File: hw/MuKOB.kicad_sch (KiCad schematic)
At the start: 137 parts, among them J1 UART0 IO01, J10 IO_EX, J11 SPKR_L, J12 SPKR_R, J13 UI 20-RBN, J14 AUDIO, J15 SPI-0, J16 SPI-DISP, J17 SW_MATRIX, J18 UIM 20-FCC, J19 UIM 20-RBN, J2 SERIAL-COMM, J3 KEY_SND_IF, J4 GPIO28, J5 I2C-0, J6 MicroSD-Socket w/Det, J7 KEY-PADDLE, J8 UART1 IO89, J9 UI 20-FCC, Q1 2N3904, SW1 RESET, SW2 RE-SO, SW3 UP, SW4 LF, SW5 EN, SW6 RT, SW7 DN, SW8 RE-AO, SW9 RE-BO, U1 MAX3221, U2 PicoW, U3 MCP23S08-E/SO, U4 TLV70033_SOT23-5, U5 TPA2012D2RTJT, U6 NC7WZ16P6X

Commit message: KSInf-MkIII: New  JA: Add terminal block
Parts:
- M_KSI1, M_KSI2, M_KSI3, M_KSI4: now left out of the parts list
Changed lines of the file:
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@@
   )
   (symbol (lib_id "Mechanical:MountingHole_Pad") (at 17.78 38.1 270) (unit 1)
-    (in_bom yes) (on_board yes) (dnp no) (fields_autoplaced)
+    (in_bom no) (on_board yes) (dnp no) (fields_autoplaced)
     (property "Reference" "M_KSI1" (at 21.59 37.465 90) (do_not_autoplace)
       (effects (font (size 1.27 1.27)) (justify left))
@@
   )
   (symbol (lib_id "Mechanical:MountingHole_Pad") (at 17.78 53.34 270) (unit 1)
-    (in_bom yes) (on_board yes) (dnp no) (fields_autoplaced)
+    (in_bom no) (on_board yes) (dnp no) (fields_autoplaced)
     (property "Reference" "M_KSI4" (at 21.59 52.705 90) (do_not_autoplace)
       (effects (font (size 1.27 1.27)) (justify left))
@@
   )
   (symbol (lib_id "Mechanical:MountingHole_Pad") (at 17.78 48.26 270) (unit 1)
-    (in_bom yes) (on_board yes) (dnp no) (fields_autoplaced)
+    (in_bom no) (on_board yes) (dnp no) (fields_autoplaced)
     (property "Reference" "M_KSI3" (at 21.59 47.625 90) (do_not_autoplace)
       (effects (font (size 1.27 1.27)) (justify left))
@@
   )
   (symbol (lib_id "Mechanical:MountingHole_Pad") (at 17.78 43.18 270) (unit 1)
-    (in_bom yes) (on_board yes) (dnp no) (fields_autoplaced)
+    (in_bom no) (on_board yes) (dnp no) (fields_autoplaced)
     (property "Reference" "M_KSI2" (at 21.59 42.545 90) (do_not_autoplace)
       (effects (font (size 1.27 1.27)) (justify left))

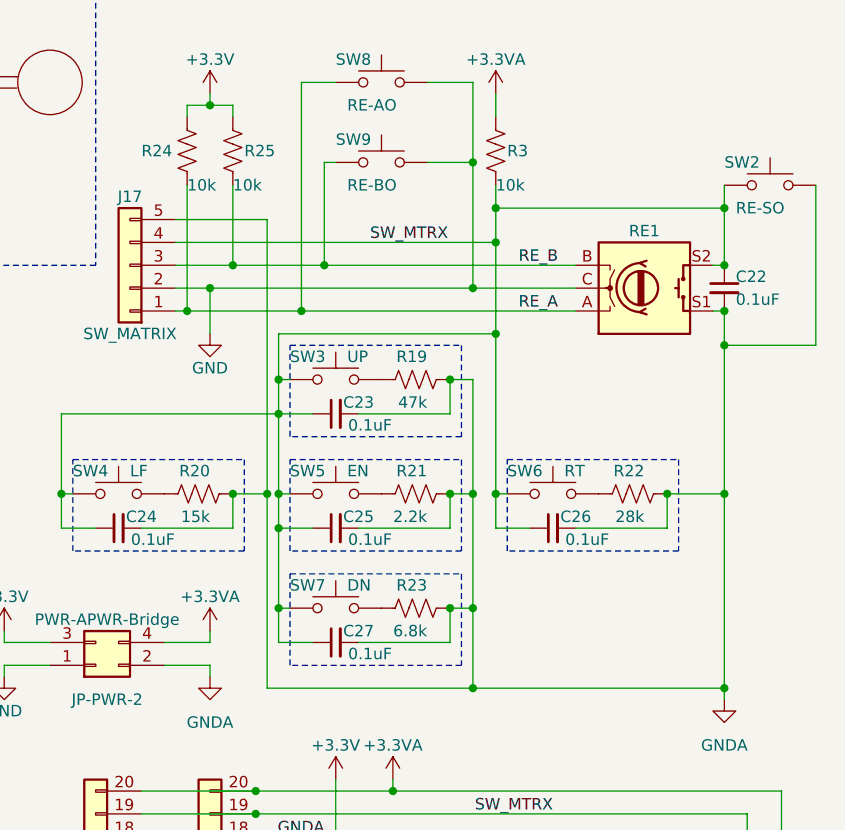
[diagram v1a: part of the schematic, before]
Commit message: KS-MkIV: Pinout for bridge and mini-sounder update.
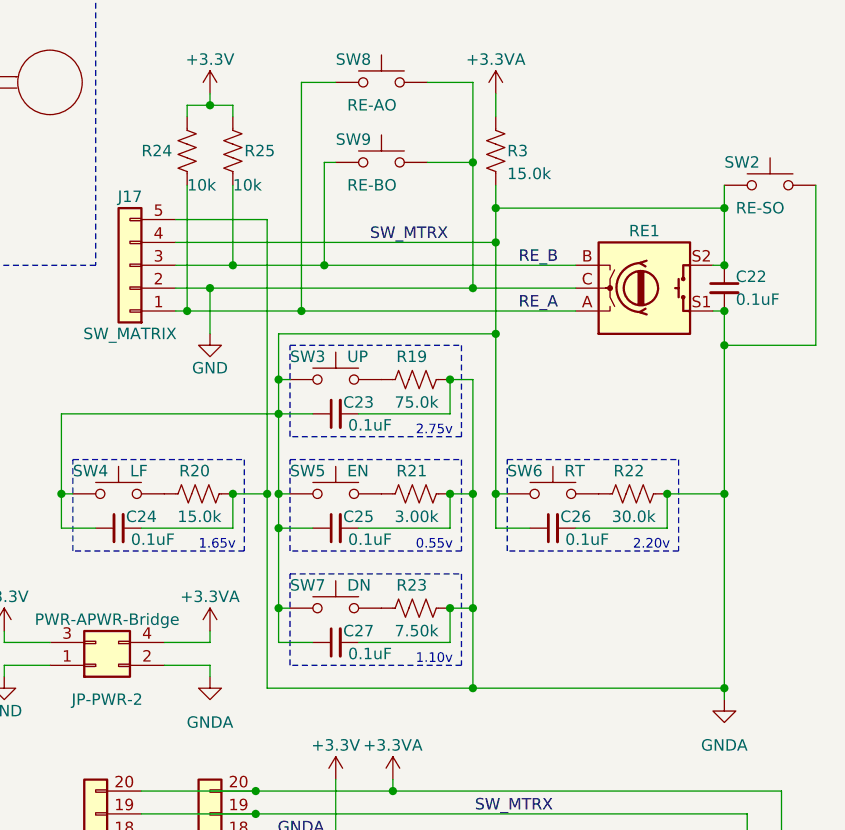
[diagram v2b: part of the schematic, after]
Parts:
- R19: value 47k -> 75.0k
- R20: value 15k -> 15.0k
- R21: value 2.2k -> 3.00k
- R22: value 28k -> 30.0k
- R23: value 6.8k -> 7.50k
- R3: value 10k -> 15.0k
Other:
- note added: "0.55v"
- note added: "1.10v"
- note added: "1.65v"
- note added: "2.20v"
- note added: "2.75v"
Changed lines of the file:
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@@
     (title "MuKOB - Device")
     (date "2024-01-16")
-    (rev "1.0")
+    (rev "1.0a")
     (company "Silky-Design (AESilky)")
     (comment 1 "Copyright 2023-24 AESilky")
@@
     (effects (font (size 1.27 1.27)) (justify left bottom))
   )
+  (text "2.20v" (at 392.43 151.13 0)
+    (effects (font (size 1.0668 1.0668)) (justify left bottom))
+  )
   (text "RES" (at 33.02 254 0)
     (effects (font (size 1.27 1.27)) (justify left bottom))
@@
     (effects (font (size 1.27 1.27)) (justify left bottom))
   )
+  (text "1.10v" (at 368.3 163.83 0)
+    (effects (font (size 1.0668 1.0668)) (justify left bottom))
+  )
   (text "VCC" (at 27.94 63.5 0)
     (effects (font (size 1.27 1.27)) (justify right bottom))
@@
     (effects (font (size 2.54 2.54) (thickness 0.508) bold) (justify left bottom))
   )
+  (text "0.55v" (at 368.3 151.13 0)
+    (effects (font (size 1.0668 1.0668)) (justify left bottom))
+  )
+  (text "2.75v" (at 368.3 138.43 0)
+    (effects (font (size 1.0668 1.0668)) (justify left bottom))
+  )
   (text "CS-" (at 33.02 259.08 0)
     (effects (font (size 1.27 1.27)) (justify left bottom))
@@
     (effects (font (size 1.27 1.27)) (justify left bottom))
   )
+  (text "1.65v" (at 344.17 151.13 0)
+    (effects (font (size 1.0668 1.0668)) (justify left bottom))
+  )
   (text "1/4in Key/Paddle Jack\n(Same as ICOM IC-7300)" (at 260.35 114.3 0)
     (effects (font (size 1.27 1.27)) (justify right bottom))
@@
       (effects (font (size 1.27 1.27)) (justify left))
     )
-    (property "Value" "10k" (at 377.19 110.49 0)
+    (property "Value" "15.0k" (at 378.46 109.22 0)
       (effects (font (size 1.27 1.27)) (justify left))
     )
@@
       (effects (font (size 1.27 1.27)) (justify right))
     )
-    (property "Value" "15k" (at 345.44 147.32 90)
+    (property "Value" "15.0k" (at 346.71 147.32 90)
       (effects (font (size 1.27 1.27)) (justify right))
     )
@@
       (effects (font (size 1.27 1.27)) (justify right))
     )
-    (property "Value" "6.8k" (at 369.57 160.02 90)
+    (property "Value" "7.50k" (at 370.84 160.02 90)
       (effects (font (size 1.27 1.27)) (justify right))
     )
@@
       (effects (font (size 1.27 1.27)) (justify right))
     )
-    (property "Value" "2.2k" (at 369.57 147.32 90)
+    (property "Value" "3.00k" (at 370.84 147.32 90)
       (effects (font (size 1.27 1.27)) (justify right))
     )
@@
       (effects (font (size 1.27 1.27)) (justify right))
     )
-    (property "Value" "47k" (at 369.57 134.62 90)
+    (property "Value" "75.0k" (at 370.84 134.62 90)
       (effects (font (size 1.27 1.27)) (justify right))
     )
@@
       (effects (font (size 1.27 1.27)) (justify right))
     )
-    (property "Value" "28k" (at 393.7 147.32 90)
+    (property "Value" "30.0k" (at 394.97 147.32 90)
       (effects (font (size 1.27 1.27)) (justify right))
     )

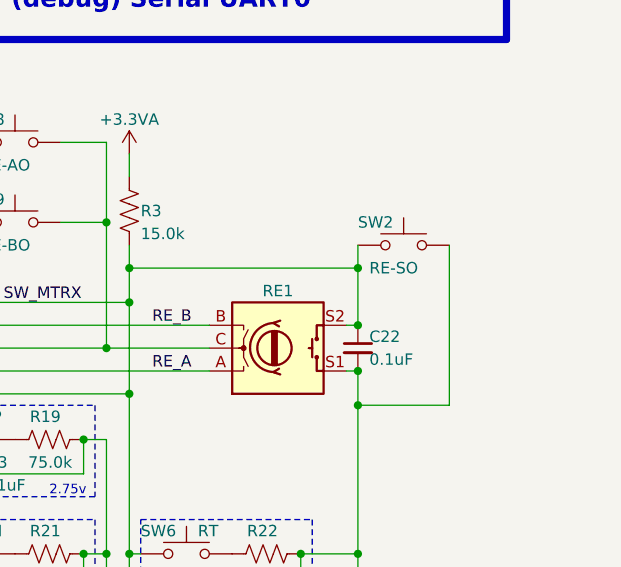
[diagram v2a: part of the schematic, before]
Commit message: MuKOB: rev b, update UI Switch res values to match Scores SW Board.
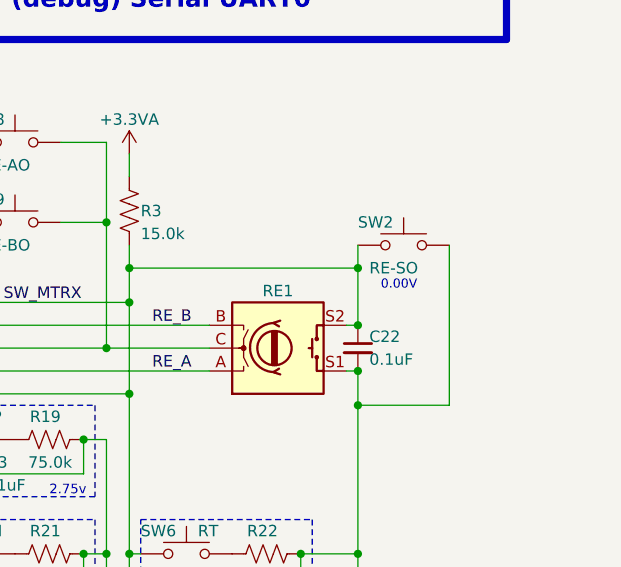
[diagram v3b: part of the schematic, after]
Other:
- note added: "0.00V"
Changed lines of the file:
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@@
     (title "MuKOB - Device")
     (date "2024-01-16")
-    (rev "1.0a")
+    (rev "1.0b")
     (company "Silky-Design (AESilky)")
     (comment 1 "Copyright 2023-24 AESilky")
@@
     (effects (font (size 1.27 1.27)) (justify right bottom))
   )
+  (text "0.00V" (at 405.13 115.57 0)
+    (effects (font (size 1.016 1.016)) (justify left bottom))
+  )
   (text "RX" (at 20.32 152.4 0)
